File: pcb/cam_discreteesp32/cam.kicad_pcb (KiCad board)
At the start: 4 copper layers, 75 x 65 mm, 113 parts, among them J1 Conn_Coaxial, J2 Power In, J3 CONN_PRG_ESP, J4 Conn_01x24_Male, J5 SIM_Card, J6 Conn_Coaxial, Q1 IRLML6402, SW1 SW_Push, SW2 SW_Push, U1 TPS22810, U10 W25Q128JVS, U11 LY68L6400, U12 SRV05-4, U13 SIM800C, U2 FDC610, U3 XC6206-12, U4 XC6206-28, U5 LTC3103, U6 INA226, U7 ESP32-D0WD, U8 MP2307, U9 MAX7321, Y1 32.768kHz, Y2 40Mhz

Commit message: Finished PCB for ESP32-S2
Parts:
- removed SW1, SW2: SW_Push, Elktown Footprints:smd_2pole_pushbtn
- removed U9: MAX7321, Package_SO:QSOP-16_3.9x4.9mm_P0.635mm
- added J7: JTAG, Connector_PinHeader_1.27mm:PinHeader_2x05_P1.27mm_Vertical, F.Cu at (132.8, 63.2)
- added R28: 0, Resistor_SMD:R_0603_1608Metric, F.Cu at (141.1, 73.8)
- added R29: 10k, Resistor_SMD:R_0603_1608Metric, F.Cu at (154.1, 75.3)
- added R30: 4.7k, Resistor_SMD:R_0603_1608Metric, F.Cu at (142.9, 64.5)
- added R31: 4.7k, Resistor_SMD:R_0603_1608Metric, F.Cu at (142.9, 66.8)
- added R32: 10k, Resistor_SMD:R_0603_1608Metric, F.Cu at (165.2, 112.7)
- C14, C15: value 270p -> 1u
- C20: footprint Capacitor_SMD:C_1206_3216Metric -> Capacitor_SMD:C_0603_1608Metric
- C23, C6: footprint Capacitor_SMD:C_0805_2012Metric -> Capacitor_SMD:C_0603_1608Metric
- C28: value 1u -> 100n; footprint Capacitor_SMD:C_0805_2012Metric -> Capacitor_SMD:C_0603_1608Metric
- C3: value 3.3n -> 100p
- C34: value 100p -> 100n
- C4: value 10n -> 1u
- J3: value CONN_PRG_ESP -> PRGR; footprint Connector_JST:JST_XH_B5B-XH-A_1x05_P2.50mm_Vertical -> Connector_PinHeader_1.27mm:PinHeader_2x03_P1.27mm_Vertical
- R1: value 20k -> 0
- U7: value ESP32-D0WD -> ESP32-S2; footprint Elktown Footprints:QFN35P500X500X90-49N -> Package_DFN_QFN:QFN-56-1EP_7x7mm_P0.4mm_EP5.6x5.6mm_ThermalVias
- moved C39 34.7 mm to (160.7, 75.8), turned to 0 degrees
- moved R19 34.2 mm to (161.7, 84.7), turned to 270 degrees
- moved R18 33.4 mm to (161.7, 81.1), turned to 270 degrees
- moved R14 31.8 mm to (112.0, 76.7), turned to 180 degrees
- moved R11 30.9 mm to (112.0, 79.0), turned to 180 degrees
- moved D3 29.4 mm to (159.3, 84.7), turned to 90 degrees
- moved D2 28.4 mm to (159.4, 81.1), turned to 90 degrees
- moved C14 21.8 mm to (141.6, 83.2), turned to 90 degrees
- moved R17 19.1 mm to (153.3, 82.7)
- moved R13 14.7 mm to (160.7, 77.6)
- moved J1 13.7 mm to (123.1, 67.9), turned to 90 degrees
- moved R1 13.6 mm to (141.1, 71.5), turned to 180 degrees
- moved R2 10.0 mm to (160.7, 74.0), turned to 180 degrees
- moved C1 9.30 mm to (123.9, 71.0), turned to 0 degrees
- moved C28 8.89 mm to (139.3, 76.6), turned to 270 degrees
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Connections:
- C10 pad 2: Net-(C10-Pad2) -> /XTALN
- C12 pad 2: Net-(C12-Pad2) -> /XTAL32N
- C14 pad 1: Net-(C14-Pad1) -> VDD_SDIO
- C14 pad 2: Net-(C14-Pad2) -> GND
- C15 pad 1: Net-(C15-Pad1) -> 3V3
- C15 pad 2: Net-(C15-Pad2) -> GND
- C28 pad 1: VDD_SDIO -> 3V3
- C3 pad 1: Net-(C3-Pad1) -> 3V3
- C3 pad 2: Net-(C3-Pad2) -> GND
- C34 pad 1: 3V3 -> VDD_SDIO
- C39 pad 1: 3V3 -> ~RST
- C4 pad 1: Net-(C3-Pad1) -> 3V3
- C7 pad 2: Net-(C7-Pad2) -> /XTAL32P
- J3 pad 2: PRGR_TX -> 3V3
- J3 pad 3: PRGR_RX -> PRGR_TX
- J3 pad 4: PRGRM -> GND
- J3 pad 5: GND -> PRGR_RX
- J4 pad 20: SCL -> SCL_CAM
- J4 pad 22: SDA -> SDA_CAM
- R1 pad 1: Net-(C3-Pad1) -> PRGR_RX
- R1 pad 2: Net-(C3-Pad2) -> Net-(R1-Pad2)
- R11 pad 2: SDA -> SCL_CAM
- R14 pad 2: SCL -> SDA_CAM
- R17 pad 1: PSRAM_CE -> SPICS1
- R18 pad 1: Net-(R18-Pad1) -> LED2
- R19 pad 1: Net-(R19-Pad1) -> LED1
- R3 pad 1: Net-(C7-Pad2) -> /XTAL32P
- R3 pad 2: Net-(C12-Pad2) -> /XTAL32N
- R5 pad 2: Net-(R5-Pad2) -> /XTALP
- U10 pad 1: SD_CMD -> SPICS0
- U10 pad 6: SD_CLK -> SPICLK
- U11 pad 1: PSRAM_CE -> SPICS1
- U11 pad 6: PSRAM_SCLK -> SPICLK
- U6 pad 4: SDA -> SDA_AUX
- U6 pad 5: SCL -> SCL_AUX
- U7 pad 10: CSI_D5 -> CSI_D7
- U7 pad 11: CSI_PCLK -> CSI_MCLK
- U7 pad 12: Net-(C7-Pad2) -> CSI_D6
- U7 pad 13: Net-(C12-Pad2) -> CSI_D5
- U7 pad 14: CSI_D4 -> CSI_PCLK
- U7 pad 15: SDA -> CSI_D4
- U7 pad 16: SCL -> CSI_D0
- U7 pad 17: CSI_D0 -> CSI_D3
- U7 pad 18: Net-(U7-Pad18) -> CSI_D1
- U7 pad 19: 3V3 -> CSI_D2
- U7 pad 20: CSI_D3 -> 3V3
- U7 pad 21: CSI_D1 -> /XTAL32P
- U7 pad 22: CSI_D2 -> /XTAL32N
- U7 pad 23: PRGRM -> GSM_TX
- U7 pad 25: PSRAM_CE -> RADIO_EN
- U7 pad 26: VDD_SDIO -> CAM_EN
- U7 pad 27: PSRAM_SCLK -> 3V3
- U7 pad 28: SD_DATA2 -> CAM_RST
- U7 pad 29: SD_DATA3 -> SPICS1
- U7 pad 30: SD_CMD -> VDD_SDIO
- U7 pad 31: SD_CLK -> SD_DATA3
- U7 pad 32: SD_DATA0 -> SD_DATA2
- U7 pad 33: SD_DATA1 -> SPICS0
- U7 pad 34: GSM_TX -> SPICLK
- U7 pad 35: CSI_VSYNC -> SD_DATA1
- U7 pad 36: CSI_HSYNC -> SD_DATA0
- U7 pad 37: 3V3 -> GSM_PWRKEY
- U7 pad 38: CSI_D7 -> LED2
- U7 pad 39: CSI_MCLK -> LED1
- U7 pad 40: PRGR_TX -> SCL_AUX
- U7 pad 41: PRGR_RX -> SDA_AUX
- U7 pad 42: CSI_D6 -> Net-(U7-Pad42)
- U7 pad 43: 3V3 -> TCK
- U7 pad 44: Net-(C10-Pad2) -> TDO
- U7 pad 45: Net-(R5-Pad2) -> 3V3
- U7 pad 46: 3V3 -> TDI
- U7 pad 47: Net-(C3-Pad2) -> TMS
- U7 pad 48: Net-(C3-Pad1) -> Net-(R28-Pad2)
- U7 pad 49: GND -> Net-(R1-Pad2)
- U7 pad 5: Net-(C14-Pad1) -> PRGRM
- U7 pad 6: Net-(C14-Pad2) -> SDA_CAM
- U7 pad 7: Net-(C15-Pad1) -> SCL_CAM
- U7 pad 8: Net-(C15-Pad2) -> CSI_VSYNC
- U7 pad 9: ~RST -> CSI_HSYNC
- Y1 pad 1: Net-(C7-Pad2) -> /XTAL32P
- Y1 pad 2: Net-(C12-Pad2) -> /XTAL32N
- Y2 pad 1: Net-(C10-Pad2) -> /XTALN
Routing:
- net SDA: track 82.1 -> 0.00 mm, vias 3 -> 0
- net SCL: track 76.1 -> 0.00 mm, vias 2 -> 0
- net SDA_CAM: track 0.00 -> 33.9 mm
- net SCL_CAM: track 0.00 -> 32.6 mm
- net LED1: track 0.00 -> 30.8 mm, vias 0 -> 2
- net CSI_D6: track 59.0 -> 31.0 mm
- net CSI_MCLK: track 58.6 -> 31.2 mm
- net CSI_HSYNC: track 56.9 -> 29.8 mm
- net CSI_D7: track 58.6 -> 31.8 mm
- net LED2: track 0.00 -> 26.5 mm, vias 0 -> 2
- net PRGRM: track 40.4 -> 66.3 mm, vias 2 -> 5
- net /XTAL32P: track 0.00 -> 25.9 mm
- net CAM_EN: track 11.4 -> 35.9 mm, vias 0 -> 2
- net SDA_AUX: track 0.00 -> 22.7 mm, vias 0 -> 2
- net Net-(R32-Pad1): track 0.00 -> 22.3 mm
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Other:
- board text added: "CAM Rev. B - 12/28/2020 elktown-labs.com"
- board text removed: "CAM Rev. A - 11/30/2020 elktown-labs.com"
- board text removed: "Prgrm"
- board text removed: "Reset"
- board text removed: "Serial/ISP Connector"

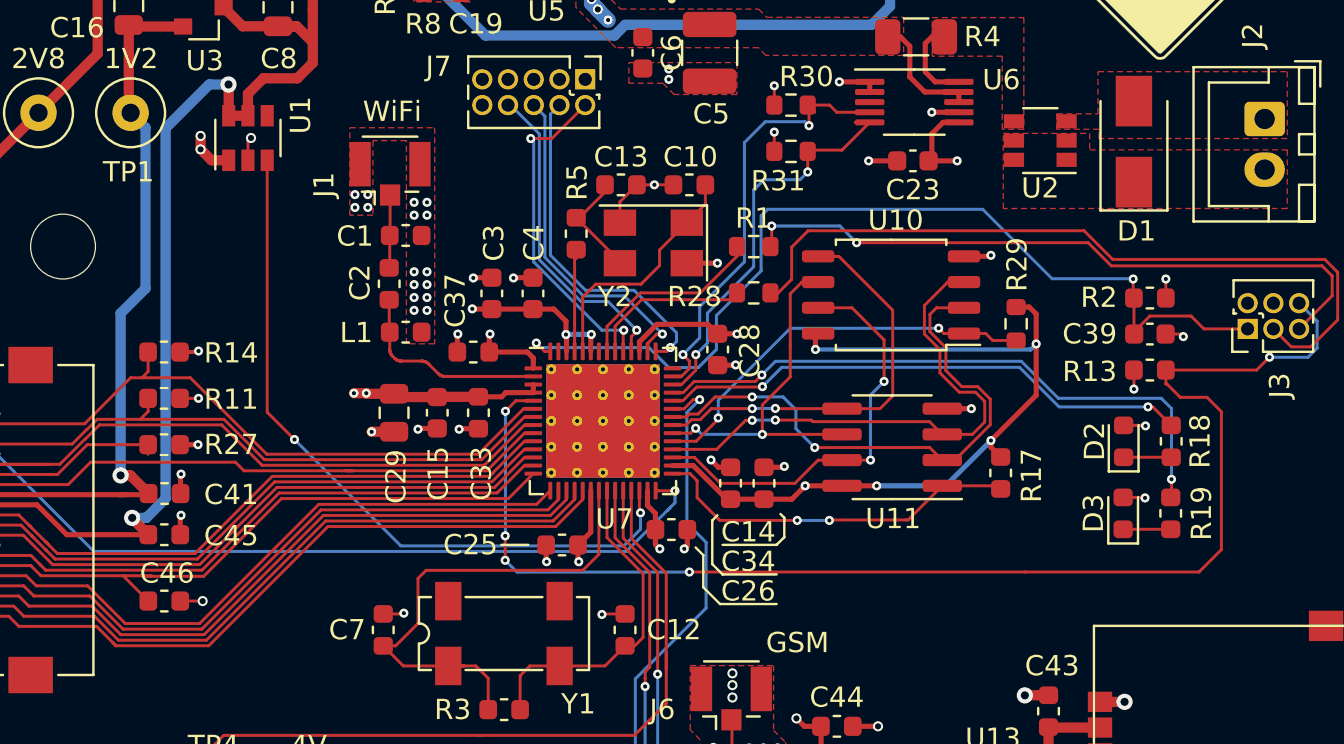
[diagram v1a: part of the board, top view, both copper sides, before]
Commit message: Minor fixed to ESP-S2 pcb
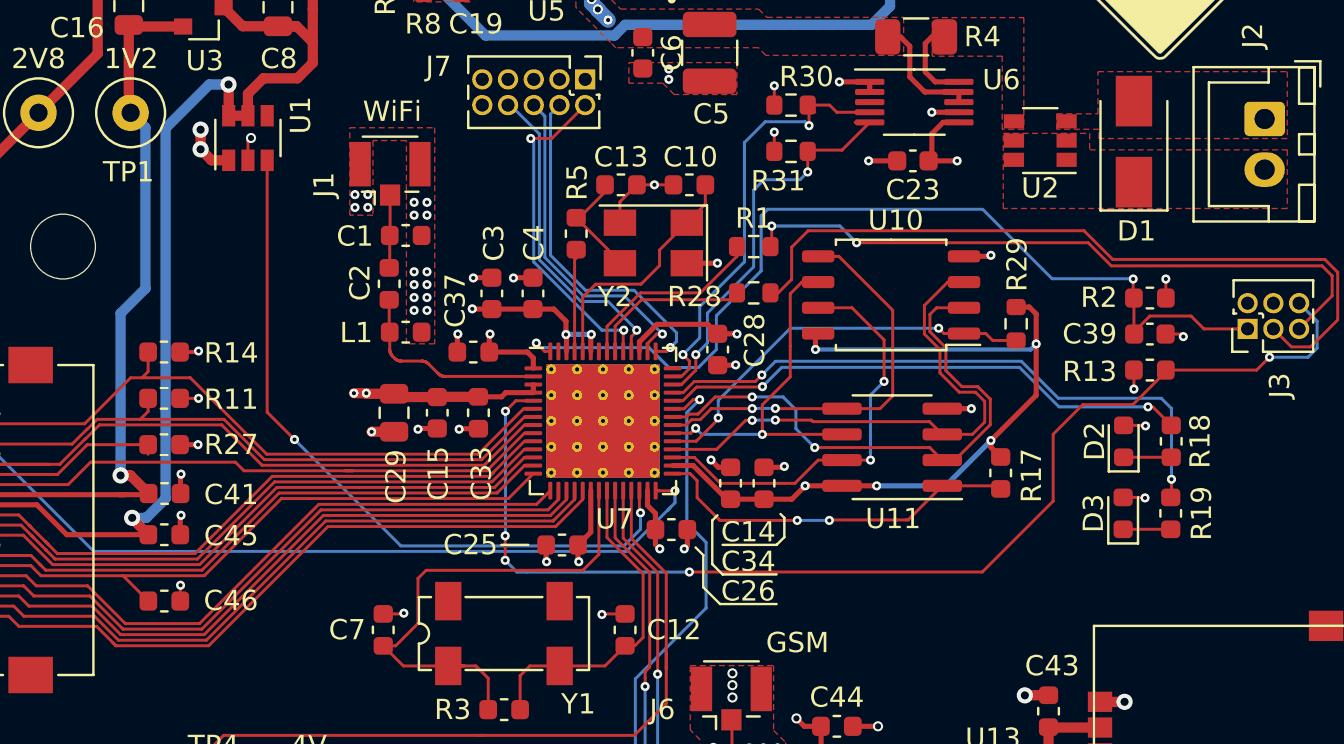
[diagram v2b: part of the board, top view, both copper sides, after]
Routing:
- net PRGRM: track 66.3 -> 58.4 mm

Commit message: More optimizations to pcb
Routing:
- net Net-(R1-Pad2): track 9.56 -> 10.3 mm

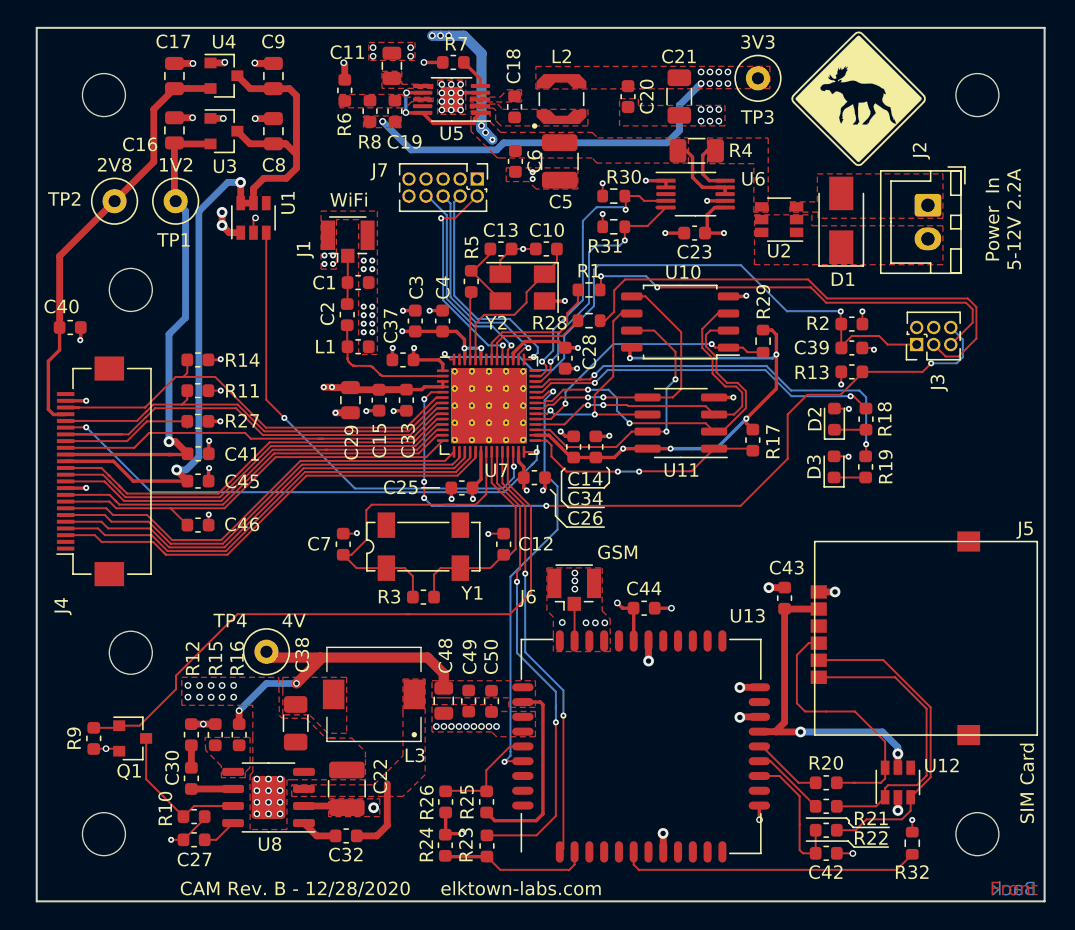
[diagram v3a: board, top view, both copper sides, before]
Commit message: Fixed connection / layout of flash / ram chips
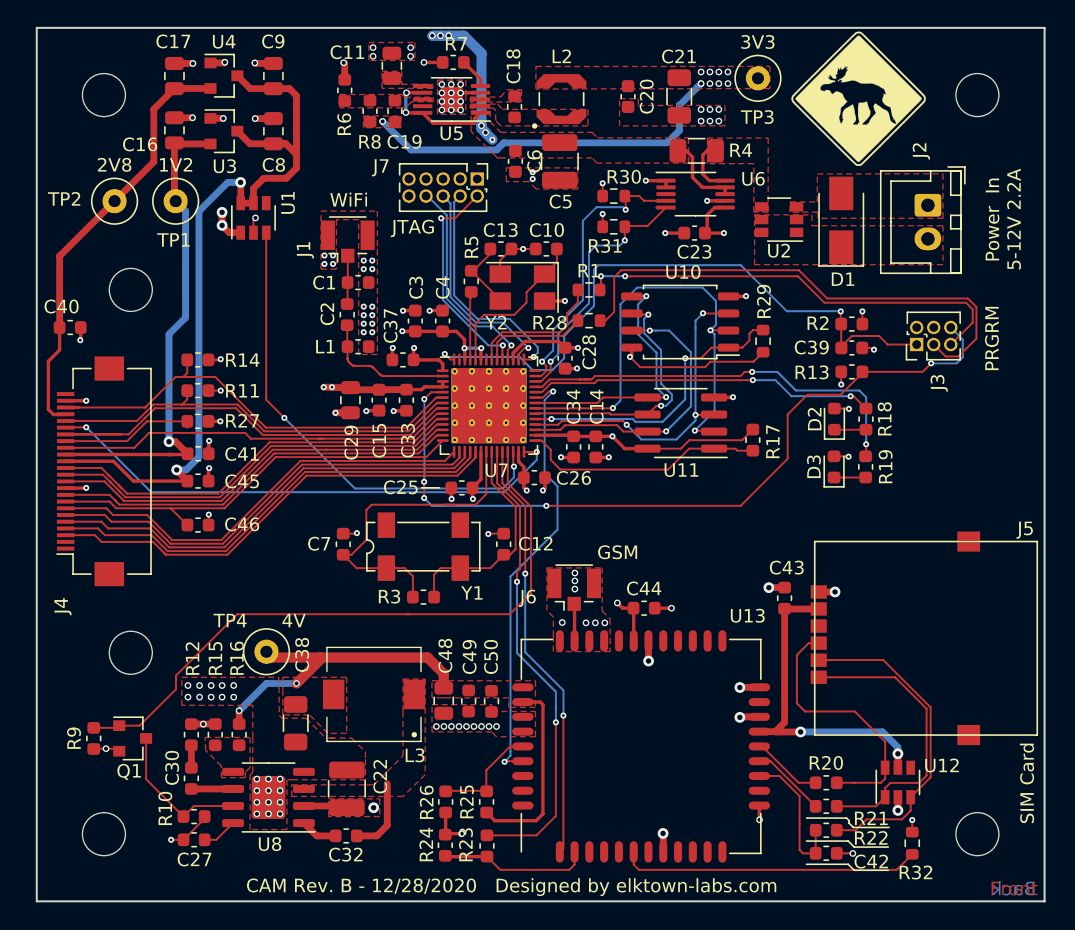
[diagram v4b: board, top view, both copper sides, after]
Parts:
- turned C14 to 270 degrees
- turned C34 to 270 degrees
- turned R29 to 270 degrees
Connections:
- U10 pad 2: SD_DATA0 -> SD_DATA1
- U10 pad 5: SD_DATA1 -> SD_DATA0
- U11 pad 2: SD_DATA0 -> SD_DATA1
- U11 pad 5: SD_DATA1 -> SD_DATA0
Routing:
- net SD_DATA1: track 20.9 -> 35.8 mm, vias 2 -> 3
- net SD_DATA0: track 28.1 -> 20.1 mm
- net VDD_SDIO: track 39.0 -> 35.3 mm, vias 5 -> 2
- net SPICLK: track 17.7 -> 20.1 mm
- net SPICS0: track 20.1 -> 22.0 mm
- net SD_DATA2: track 26.4 -> 24.7 mm, vias 2 -> 3
- net PRGR_TX: track 37.5 -> 38.7 mm
- net SD_DATA3: track 20.9 -> 21.8 mm
- net LED2: track 26.5 -> 25.9 mm
- net SPICS1: track 18.5 -> 18.2 mm, vias 2 -> 0
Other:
- board text added: "CAM Rev. B - 12/28/2020 Designed by elktown-labs.com"
- board text added: "JTAG"
- board text added: "PRGRM"
- board text removed: "CAM Rev. B - 12/28/2020 elktown-labs.com"
